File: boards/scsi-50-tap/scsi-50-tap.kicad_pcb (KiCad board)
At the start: 4 copper layers, 121.4 x 109.4 mm, 9 parts, among them J1 SIDE-A, J2 SIDE-B, J3 TAP-OUT

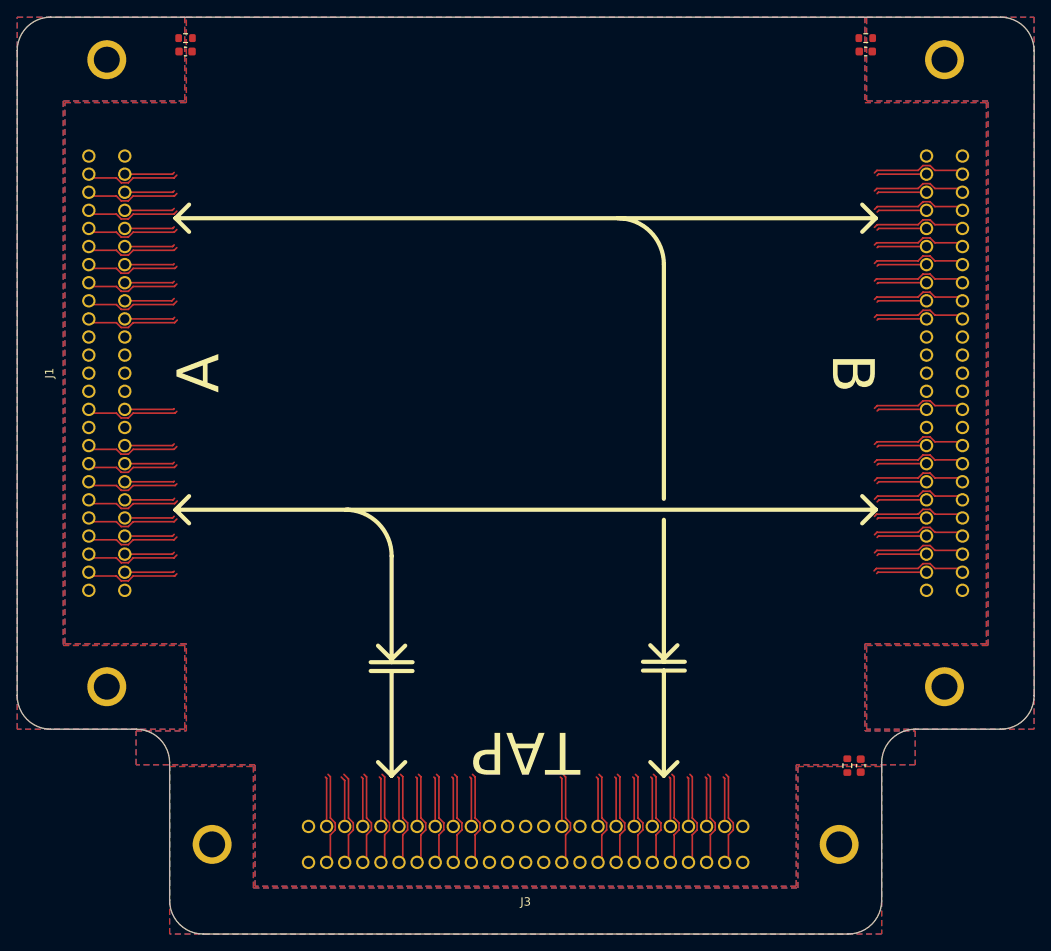
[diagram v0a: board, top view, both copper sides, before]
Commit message: hardware: scsi-tap: 50: Updated the 50-pin scsi tap, still needs some work
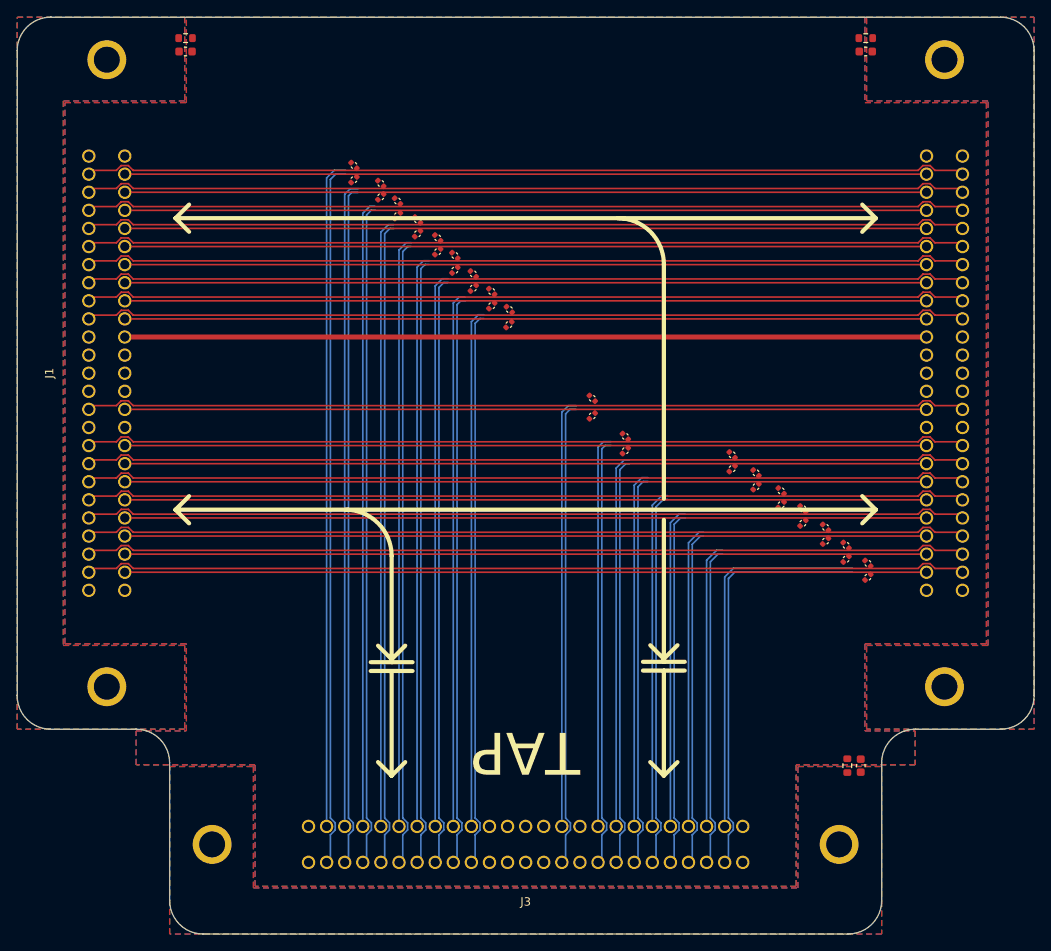
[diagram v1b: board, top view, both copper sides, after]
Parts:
- added C10: 16pF, Capacitor_SMD:C_0402_1005Metric, F.Cu at (87.1, 81.7)
- added C11: 16pF, Capacitor_SMD:C_0402_1005Metric, F.Cu at (87.1, 83.3)
- added C12: 16pF, Capacitor_SMD:C_0402_1005Metric, F.Cu at (89.5, 83.8)
- added C13: 16pF, Capacitor_SMD:C_0402_1005Metric, F.Cu at (89.5, 85.5)
- added C14: 16pF, Capacitor_SMD:C_0402_1005Metric, F.Cu at (91.5, 86.0)
- added C15: 16pF, Capacitor_SMD:C_0402_1005Metric, F.Cu at (91.5, 87.7)
- added C16: 16pF, Capacitor_SMD:C_0402_1005Metric, F.Cu at (93.8, 88.2)
- added C17: 16pF, Capacitor_SMD:C_0402_1005Metric, F.Cu at (93.8, 89.8)
- added C18: 16pF, Capacitor_SMD:C_0402_1005Metric, F.Cu at (96.0, 90.2)
- added C19: 16pF, Capacitor_SMD:C_0402_1005Metric, F.Cu at (96.0, 92.0)
- added C20: 16pF, Capacitor_SMD:C_0402_1005Metric, F.Cu at (98.0, 92.4)
- added C21: 16pF, Capacitor_SMD:C_0402_1005Metric, F.Cu at (98.0, 94.2)
- added C22: 16pF, Capacitor_SMD:C_0402_1005Metric, F.Cu at (108.0, 103.0)
- added C23: 16pF, Capacitor_SMD:C_0402_1005Metric, F.Cu at (108.0, 105.1)
- added C24: 16pF, Capacitor_SMD:C_0402_1005Metric, F.Cu at (111.9, 107.5)
- added C25: 16pF, Capacitor_SMD:C_0402_1005Metric, F.Cu at (111.9, 109.2)
- added C26: 16pF, Capacitor_SMD:C_0402_1005Metric, F.Cu at (124.7, 109.8)
- added C27: 16pF, Capacitor_SMD:C_0402_1005Metric, F.Cu at (124.7, 111.4)
- added C28: 16pF, Capacitor_SMD:C_0402_1005Metric, F.Cu at (127.5, 111.9)
- added C29: 16pF, Capacitor_SMD:C_0402_1005Metric, F.Cu at (127.5, 113.5)
- added C30: 16pF, Capacitor_SMD:C_0402_1005Metric, F.Cu at (130.5, 114.0)
- added C31: 16pF, Capacitor_SMD:C_0402_1005Metric, F.Cu at (130.5, 115.7)
- added C32: 16pF, Capacitor_SMD:C_0402_1005Metric, F.Cu at (133.1, 116.2)
- added C33: 16pF, Capacitor_SMD:C_0402_1005Metric, F.Cu at (133.1, 117.9)
- added C34: 16pF, Capacitor_SMD:C_0402_1005Metric, F.Cu at (135.8, 118.4)
- added C35: 16pF, Capacitor_SMD:C_0402_1005Metric, F.Cu at (135.8, 120.0)
- added C36: 16pF, Capacitor_SMD:C_0402_1005Metric, F.Cu at (138.2, 120.5)
- added C37: 16pF, Capacitor_SMD:C_0402_1005Metric, F.Cu at (138.2, 122.2)
- added C38: 16pF, Capacitor_SMD:C_0402_1005Metric, F.Cu at (140.8, 122.7)
- added C39: 16pF, Capacitor_SMD:C_0402_1005Metric, F.Cu at (140.8, 124.3)
- added C4: 16pF, Capacitor_SMD:C_0402_1005Metric, F.Cu at (79.5, 75.2)
- added C5: 16pF, Capacitor_SMD:C_0402_1005Metric, F.Cu at (79.5, 76.9)
- added C6: 16pF, Capacitor_SMD:C_0402_1005Metric, F.Cu at (82.7, 77.3)
- added C7: 16pF, Capacitor_SMD:C_0402_1005Metric, F.Cu at (82.7, 79.0)
- added C8: 16pF, Capacitor_SMD:C_0402_1005Metric, F.Cu at (84.7, 79.5)
- added C9: 16pF, Capacitor_SMD:C_0402_1005Metric, F.Cu at (84.7, 81.2)
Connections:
- J1 pad 10: /SCSI-A.DBP+ -> /SCSI-P.DBP+
- J1 pad 15: /SCSI-A.ATN+ -> /SCSI-P.ATN+
- J1 pad 17: /SCSI-A.BSY+ -> /SCSI-P.BSY+
- J1 pad 18: /SCSI-A.ACK+ -> /SCSI-P.ACK+
- J1 pad 19: /SCSI-A.RST+ -> /SCSI-P.RST+
- J1 pad 2: /SCSI-A.DB0+ -> /SCSI-P.DB0+
- J1 pad 20: /SCSI-A.MSG+ -> /SCSI-P.MSG+
- J1 pad 21: /SCSI-A.SEL+ -> /SCSI-P.SEL+
- J1 pad 22: /SCSI-A.CD+ -> /SCSI-P.CD+
- J1 pad 23: /SCSI-A.REQ+ -> /SCSI-P.REQ+
- J1 pad 24: /SCSI-A.IO+ -> /SCSI-P.IO+
- J1 pad 27: /SCSI-A.DB0- -> /SCSI-P.DB0-
- J1 pad 28: /SCSI-A.DB1- -> /SCSI-P.DB1-
- J1 pad 29: /SCSI-A.DB2- -> /SCSI-P.DB2-
- J1 pad 3: /SCSI-A.DB1+ -> /SCSI-P.DB1+
- J1 pad 30: /SCSI-A.DB3- -> /SCSI-P.DB3-
- J1 pad 31: /SCSI-A.DB4- -> /SCSI-P.DB4-
- J1 pad 32: /SCSI-A.DB5- -> /SCSI-P.DB5-
- J1 pad 33: /SCSI-A.DB6- -> /SCSI-P.DB6-
- J1 pad 34: /SCSI-A.DB7- -> /SCSI-P.DB7-
- J1 pad 35: /SCSI-A.DBP- -> /SCSI-P.DBP-
- J1 pad 4: /SCSI-A.DB2+ -> /SCSI-P.DB2+
- J1 pad 40: /SCSI-A.ATN- -> /SCSI-P.ATN-
- J1 pad 42: /SCSI-A.BSY- -> /SCSI-P.BSY-
- J1 pad 43: /SCSI-A.ACK- -> /SCSI-P.ACK-
- J1 pad 44: /SCSI-A.RST- -> /SCSI-P.RST-
- J1 pad 45: /SCSI-A.MSG- -> /SCSI-P.MSG-
- J1 pad 46: /SCSI-A.SEL- -> /SCSI-P.SEL-
- J1 pad 47: /SCSI-A.CD- -> /SCSI-P.CD-
- J1 pad 48: /SCSI-A.REQ- -> /SCSI-P.REQ-
- J1 pad 49: /SCSI-A.IO- -> /SCSI-P.IO-
- J1 pad 5: /SCSI-A.DB3+ -> /SCSI-P.DB3+
- J1 pad 6: /SCSI-A.DB4+ -> /SCSI-P.DB4+
- J1 pad 7: /SCSI-A.DB5+ -> /SCSI-P.DB5+
- J1 pad 8: /SCSI-A.DB6+ -> /SCSI-P.DB6+
- J1 pad 9: /SCSI-A.DB7+ -> /SCSI-P.DB7+
- J2 pad 10: /SCSI-B.DBP+ -> /SCSI-P.DBP+
- J2 pad 15: /SCSI-B.ATN+ -> /SCSI-P.ATN+
- J2 pad 17: /SCSI-B.BSY+ -> /SCSI-P.BSY+
- J2 pad 18: /SCSI-B.ACK+ -> /SCSI-P.ACK+
- J2 pad 19: /SCSI-B.RST+ -> /SCSI-P.RST+
- J2 pad 2: /SCSI-B.DB0+ -> /SCSI-P.DB0+
- J2 pad 20: /SCSI-B.MSG+ -> /SCSI-P.MSG+
- J2 pad 21: /SCSI-B.SEL+ -> /SCSI-P.SEL+
- J2 pad 22: /SCSI-B.CD+ -> /SCSI-P.CD+
- J2 pad 23: /SCSI-B.REQ+ -> /SCSI-P.REQ+
- J2 pad 24: /SCSI-B.IO+ -> /SCSI-P.IO+
- J2 pad 27: /SCSI-B.DB0- -> /SCSI-P.DB0-
- J2 pad 28: /SCSI-B.DB1- -> /SCSI-P.DB1-
- J2 pad 29: /SCSI-B.DB2- -> /SCSI-P.DB2-
- J2 pad 3: /SCSI-B.DB1+ -> /SCSI-P.DB1+
- J2 pad 30: /SCSI-B.DB3- -> /SCSI-P.DB3-
- J2 pad 31: /SCSI-B.DB4- -> /SCSI-P.DB4-
- J2 pad 32: /SCSI-B.DB5- -> /SCSI-P.DB5-
- J2 pad 33: /SCSI-B.DB6- -> /SCSI-P.DB6-
- J2 pad 34: /SCSI-B.DB7- -> /SCSI-P.DB7-
- J2 pad 35: /SCSI-B.DBP- -> /SCSI-P.DBP-
- J2 pad 4: /SCSI-B.DB2+ -> /SCSI-P.DB2+
- J2 pad 40: /SCSI-B.ATN- -> /SCSI-P.ATN-
- J2 pad 42: /SCSI-B.BSY- -> /SCSI-P.BSY-
- J2 pad 43: /SCSI-B.ACK- -> /SCSI-P.ACK-
- J2 pad 44: /SCSI-B.RST- -> /SCSI-P.RST-
- J2 pad 45: /SCSI-B.MSG- -> /SCSI-P.MSG-
- J2 pad 46: /SCSI-B.SEL- -> /SCSI-P.SEL-
- J2 pad 47: /SCSI-B.CD- -> /SCSI-P.CD-
- J2 pad 48: /SCSI-B.REQ- -> /SCSI-P.REQ-
- J2 pad 49: /SCSI-B.IO- -> /SCSI-P.IO-
- J2 pad 5: /SCSI-B.DB3+ -> /SCSI-P.DB3+
- J2 pad 6: /SCSI-B.DB4+ -> /SCSI-P.DB4+
- J2 pad 7: /SCSI-B.DB5+ -> /SCSI-P.DB5+
- J2 pad 8: /SCSI-B.DB6+ -> /SCSI-P.DB6+
- J2 pad 9: /SCSI-B.DB7+ -> /SCSI-P.DB7+
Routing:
- net /SCSI-P.DB4-: track 0.00 -> 105.6 mm
- net /SCSI-P.DB0-: track 0.00 -> 105.6 mm
- net /SCSI-P.SEL-: track 0.00 -> 105.6 mm
- net /SCSI-P.RST-: track 0.00 -> 105.6 mm
- net /SCSI-P.REQ-: track 0.00 -> 105.6 mm
- net /SCSI-P.MSG-: track 0.00 -> 105.6 mm
- net /SCSI-P.IO-: track 0.00 -> 105.6 mm
- net /SCSI-P.DB7-: track 0.00 -> 105.6 mm
- net /SCSI-P.DB5-: track 0.00 -> 105.6 mm
- net /SCSI-P.DB3-: track 0.00 -> 105.6 mm
- net /SCSI-P.DB2-: track 0.00 -> 105.6 mm
- net /SCSI-P.BSY-: track 0.00 -> 105.6 mm
- net /SCSI-P.ATN-: track 0.00 -> 105.6 mm
- net /SCSI-P.ACK-: track 0.00 -> 105.6 mm
- net /SCSI-P.DBP-: track 0.00 -> 105.6 mm
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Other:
- board text removed: "A"
- board text removed: "B"
